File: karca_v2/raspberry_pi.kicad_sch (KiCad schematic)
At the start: 10 parts, among them J7 Raspberry_pi, Q2 PN2222A, U13 M41T93

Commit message: revisions for V2.1
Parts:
- J7: footprint Connector_PinHeader_2.00mm:PinHeader_2x20_P2.00mm_Vertical -> Connector_PinSocket_2.00mm:PinSocket_2x20_P2.00mm_Vertical

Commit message: updated POS
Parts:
- U13: now not fitted; now left out of the parts list
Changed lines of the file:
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@@
 		(unit 1)
 		(exclude_from_sim no)
-		(in_bom yes)
+		(in_bom no)
 		(on_board yes)
-		(dnp no)
+		(dnp yes)
 		(fields_autoplaced yes)
 		(property "Reference" "U13"

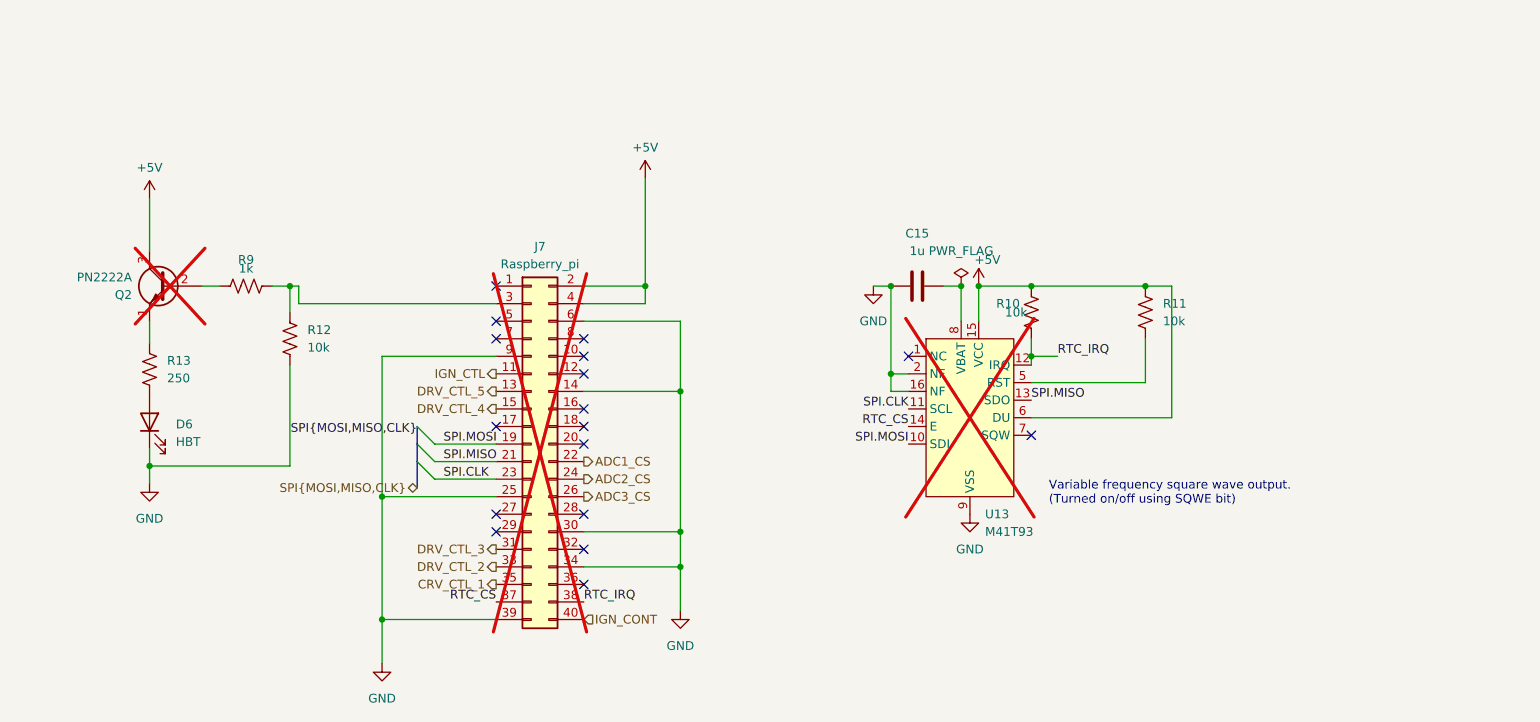
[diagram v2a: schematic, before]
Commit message: Replaced header with a smaller one, added silksreen labels, and removed secondary USB power source
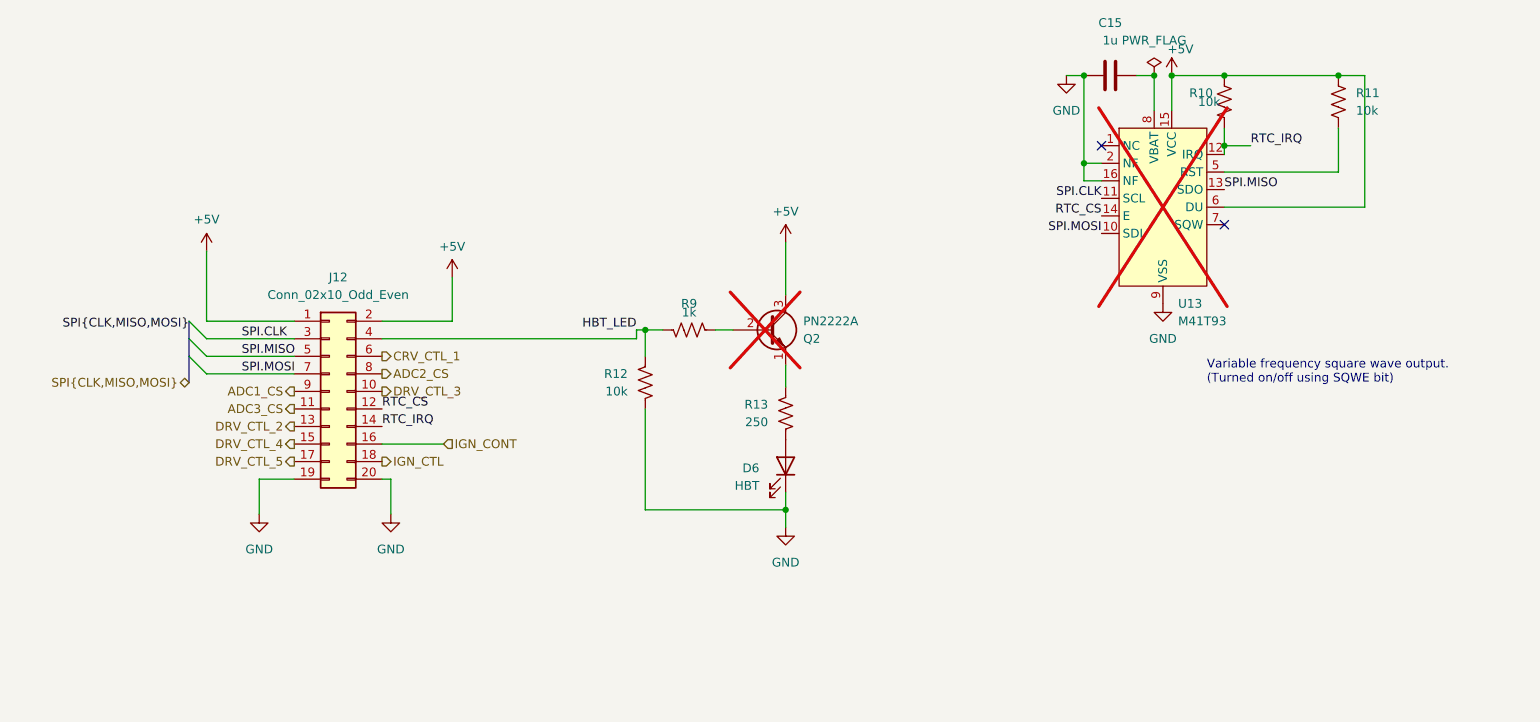
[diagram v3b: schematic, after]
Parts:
- removed J7: Raspberry_pi, Connector_PinSocket_2.00mm:PinSocket_2x20_P2.00mm_Vertical, symbol Connector_Generic_MountingPin:Conn_02x20_Odd_Even_MountingPin
- added J12: Conn_02x10_Odd_Even, Connector_PinSocket_2.54mm:PinSocket_2x10_P2.54mm_Vertical, symbol Connector_Generic:Conn_02x10_Odd_Even
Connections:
- net +5V: now also J12.1 (Pin_1), J12.2 (Pin_2)
- net ADC1_CS: now also J12.9 (Pin_9)
- net ADC2_CS: now also J12.8 (Pin_8)
- net ADC3_CS: now also J12.11 (Pin_11)
- net CRV_CTL_1: now also J12.6 (Pin_6)
- net DRV_CTL_2: now also J12.13 (Pin_13)
- net DRV_CTL_3: now also J12.10 (Pin_10)
- net DRV_CTL_4: now also J12.15 (Pin_15)
- net DRV_CTL_5: now also J12.17 (Pin_17)
- net GND: now also J12.19 (Pin_19), J12.20 (Pin_20)
- net IGN_CONT: now also J12.16 (Pin_16)
- net IGN_CTL: now also J12.18 (Pin_18)
- net RTC_CS: now also J12.12 (Pin_12)
- net RTC_IRQ: now also J12.14 (Pin_14)
- net SPI.CLK: now also J12.3 (Pin_3)
- net SPI.MISO: now also J12.5 (Pin_5)
- net SPI.MOSI: now also J12.7 (Pin_7)
- net HBT_LED: now reaches R12.2, R9.2
- net HBT_LED: now also J12.4 (Pin_4)
- no-connect marks 17 -> 2
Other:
- moved on the sheet: C15, D6, Q2, R10, R11, R12, R13, R9, U13

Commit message: restart: way too many changes made
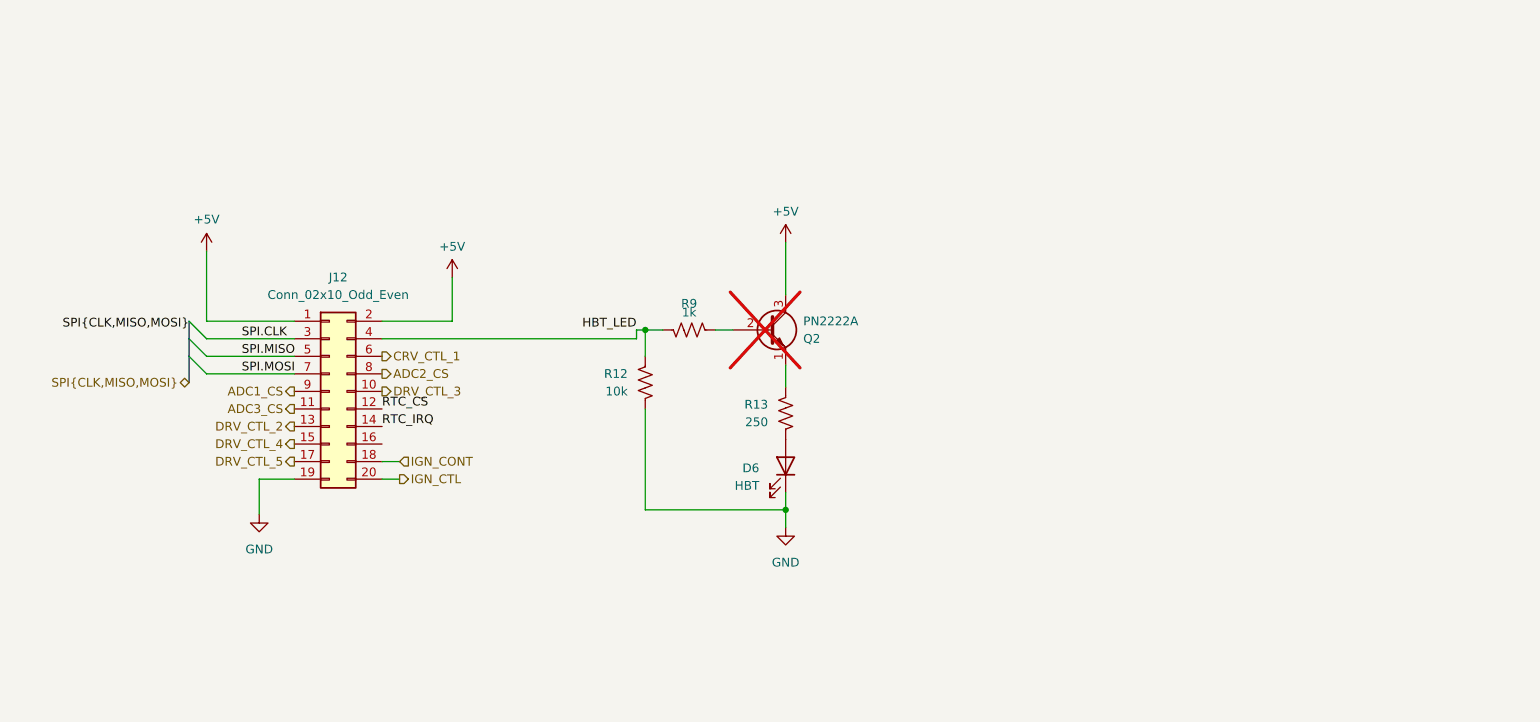
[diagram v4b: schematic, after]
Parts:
- removed C15: 1u, Capacitor_SMD:C_1206_3216Metric, symbol Device:C
- removed R10, R11: 10k, Resistor_SMD:R_1206_3216Metric, symbol Device:R_US
- removed U13: M41T93, Package_SO:SOIC-18W_7.5x11.6mm_P1.27mm, symbol karca_lib:M41T93
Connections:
- net GND: no longer J12.20 (Pin_20)
- net IGN_CONT: now also J12.18 (Pin_18); no longer J12.16 (Pin_16)
- net IGN_CTL: now also J12.20 (Pin_20); no longer J12.18 (Pin_18)
- no-connect marks 2 -> 0
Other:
- note removed: "Variable frequency square wave output. (Turned on/off using SQWE bit)"
